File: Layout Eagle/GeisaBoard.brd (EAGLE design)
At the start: 87.6 x 63.7 mm, 19 parts, among them X1 22-23-2021

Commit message: GeisaBoard layout completo (espero)
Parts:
- removed Q2: (no value), transistor-power:TO220BV
- removed R3: (no value), rcl:0204/7
- added Q1: IRF540, transistor-power:TO220BV
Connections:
- removed net N$1: DB9.1, Q2.D
- net GND: now also Q1.S; no longer DB9.5
- net LEIRASATIVAS: now also Q1.G; no longer Q2.G
- net N$2: now also DB9.5, Q1.D; no longer Q2.S, R3.1
- net VCC: now also DB9.1; no longer R3.2
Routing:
- net VCC: track 61.4 -> 93.0 mm
- net N$2: track 7.89 -> 28.5 mm
- net N$1: track 15.6 -> 0.00 mm
- net LEIRASATIVAS: track 49.3 -> 43.1 mm
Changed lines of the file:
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@@
 <layers>
 <layer number="1" name="Top" color="4" fill="1" visible="yes" active="yes"/>
-<layer number="16" name="Bottom" color="1" fill="1" visible="no" active="yes"/>
+<layer number="16" name="Bottom" color="1" fill="1" visible="yes" active="yes"/>
 <layer number="17" name="Pads" color="2" fill="1" visible="yes" active="yes"/>
 <layer number="18" name="Vias" color="2" fill="1" visible="yes" active="yes"/>
@@
 <attribute name="OC_NEWARK" value="25C3832" x="78.74" y="37.465" size="1.778" layer="27" rot="R90" display="off"/>
 </element>
-<element name="R3" library="rcl" library_urn="urn:adsk.eagle:library:334" package="0204/7" package3d_urn="urn:adsk.eagle:package:23498/1" value="" x="54.864" y="70.612" rot="R270"/>
-<element name="Q2" library="transistor-power" library_urn="urn:adsk.eagle:library:400" package="TO220BV" package3d_urn="urn:adsk.eagle:package:29484/3" value="" x="59.69" y="70.612" rot="R90"/>
+<element name="Q1" library="transistor-power" library_urn="urn:adsk.eagle:library:400" package="TO220BV" package3d_urn="urn:adsk.eagle:package:29484/3" value="IRF540" x="58.293" y="63.373"/>
 </elements>
 <signals>
-<signal name="GND" class="1">
+<signal name="GND" class="1" airwireshidden="yes">
 <contactref element="ATMEGA" pad="8"/>
 <contactref element="ATMEGA" pad="22"/>
@@
 <contactref element="JACK" pad="GNDBREAK"/>
 <contactref element="BLUETOOTH" pad="4"/>
-<contactref element="DB9" pad="5"/>
 <polygon width="0.1524" layer="16">
 <vertex x="100.838" y="-0.508"/>
@@
 <wire x1="26.67" y1="74.295" x2="26.924" y2="74.8538" width="1.016" layer="1"/>
 <wire x1="6.35" y1="57.785" x2="6.35" y2="57.658" width="1.016" layer="1"/>
+<contactref element="Q1" pad="S"/>
 </signal>
 <signal name="SPI_SCK">
@@
 <signal name="LEIRASATIVAS">
 <contactref element="ATMEGA" pad="11"/>
-<contactref element="Q2" pad="G"/>
 <wire x1="43.815" y1="40.64" x2="39.37" y2="36.195" width="0.508" layer="1"/>
 <wire x1="43.815" y1="62.992" x2="43.815" y2="40.64" width="0.508" layer="1"/>
-<wire x1="45.593" y1="64.77" x2="43.815" y2="62.992" width="0.508" layer="1"/>
-<wire x1="58.928" y1="64.77" x2="45.593" y2="64.77" width="0.508" layer="1"/>
-<wire x1="62.23" y1="68.072" x2="58.928" y2="64.77" width="0.508" layer="1"/>
+<wire x1="43.815" y1="62.992" x2="45.593" y2="64.77" width="0.508" layer="1"/>
 <wire x1="39.37" y1="36.195" x2="39.37" y2="36.068" width="0.508" layer="1"/>
+<contactref element="Q1" pad="G"/>
+<wire x1="51.816" y1="64.77" x2="55.753" y2="60.833" width="0.508" layer="1"/>
+<wire x1="45.593" y1="64.77" x2="51.816" y2="64.77" width="0.508" layer="1"/>
 </signal>
 <signal name="S0">
@@
 <wire x1="27.305" y1="38.735" x2="27.686" y2="39.116" width="0.508" layer="1"/>
 <wire x1="25.4" y1="41.402" x2="27.686" y2="39.116" width="0.508" layer="16"/>
-<wire x1="46.863" y1="58.928" x2="46.99" y2="58.928" width="0.508" layer="16"/>
 <wire x1="46.99" y1="58.928" x2="44.323" y2="58.928" width="0.508" layer="16"/>
 <wire x1="43.688" y1="59.563" x2="43.688" y2="64.135" width="0.508" layer="16"/>
@@
 <wire x1="39.497" y1="48.895" x2="39.37" y2="48.768" width="0.508" layer="1"/>
 <wire x1="44.958" y1="67.056" x2="47.752" y2="67.056" width="0.508" layer="1"/>
-<wire x1="55.88" y1="61.722" x2="76.304" y2="61.722" width="0.508" layer="16"/>
-<wire x1="50.546" y1="67.056" x2="55.88" y2="61.722" width="0.508" layer="16"/>
-<wire x1="47.752" y1="67.056" x2="50.546" y2="67.056" width="0.508" layer="16"/>
+<wire x1="74.295" y1="61.722" x2="76.304" y2="61.722" width="0.508" layer="16"/>
+<wire x1="68.961" y1="67.056" x2="74.295" y2="61.722" width="0.508" layer="16"/>
+<wire x1="47.752" y1="67.056" x2="68.961" y2="67.056" width="0.508" layer="16"/>
 <wire x1="42.545" y1="64.643" x2="44.958" y2="67.056" width="0.508" layer="1"/>
 <wire x1="42.545" y1="51.943" x2="42.545" y2="64.643" width="0.508" layer="1"/>
@@
 <wire x1="46.99" y1="36.068" x2="59.055" y2="36.068" width="0.508" layer="1"/>
 </signal>
-<signal name="VCC" class="1">
+<signal name="VCC" class="1" airwireshidden="yes">
 <contactref element="SD" pad="VCC"/>
 <contactref element="ATMEGA" pad="21"/>
@@
 <contactref element="VCC_LIGAR_BLUETOOTH" pad="MP"/>
 <contactref element="JACK" pad="PWR"/>
-<contactref element="R3" pad="2"/>
 <polygon width="0.1524" layer="1">
 <vertex x="-1.524" y="80.772"/>
@@
 <wire x1="71.882" y1="33.147" x2="67.437" y2="33.147" width="1.016" layer="16"/>
 <wire x1="67.437" y1="33.147" x2="59.436" y2="41.148" width="1.016" layer="16"/>
+<contactref element="DB9" pad="1"/>
+<wire x1="76.304" y1="67.262" x2="68.89" y2="74.676" width="1.016" layer="16"/>
+<wire x1="68.89" y1="74.676" x2="47.752" y2="74.676" width="1.016" layer="16"/>
 </signal>
 <signal name="BLUETOOTH_LIGADO">
@@
 <wire x1="41.275" y1="65.024" x2="41.275" y2="53.213" width="0.508" layer="1"/>
 <wire x1="36.068" y1="70.231" x2="41.275" y2="65.024" width="0.508" layer="1"/>
-<wire x1="9.525" y1="49.022" x2="10.2235" y2="49.7205" width="0.508" layer="1"/>
-<wire x1="6.477" y1="45.974" x2="9.525" y2="49.022" width="0.508" layer="1"/>
-<wire x1="6.223" y1="53.848" x2="10.2235" y2="53.848" width="0.508" layer="1"/>
-<wire x1="10.287" y1="53.848" x2="26.67" y2="70.231" width="0.508" layer="1"/>
+<wire x1="10.2235" y1="49.7205" x2="6.477" y2="45.974" width="0.508" layer="1"/>
+<wire x1="26.67" y1="70.231" x2="10.287" y2="53.848" width="0.508" layer="1"/>
 <wire x1="26.67" y1="70.231" x2="36.068" y2="70.231" width="0.508" layer="1"/>
-<wire x1="10.2235" y1="49.7205" x2="10.2235" y2="53.848" width="0.508" layer="1"/>
-<wire x1="10.2235" y1="53.848" x2="10.287" y2="53.848" width="0" layer="19" extent="1-1"/>
+<wire x1="10.287" y1="53.848" x2="6.223" y2="53.848" width="0.508" layer="1"/>
+<wire x1="10.287" y1="53.848" x2="10.2235" y2="53.7845" width="0.508" layer="1"/>
+<wire x1="10.2235" y1="53.7845" x2="10.2235" y2="49.7205" width="0.508" layer="1"/>
 </signal>
 <signal name="SS_ADC">
@@
 <wire x1="79.144" y1="63.102" x2="79.254" y2="62.992" width="0.508" layer="16"/>
 </signal>
-<signal name="N$1" class="1">
-<contactref element="DB9" pad="1"/>
-<contactref element="Q2" pad="D"/>
-<wire x1="73.025" y1="70.485" x2="62.23" y2="70.485" width="1.016" layer="16"/>
-<wire x1="76.295571875" y1="67.214428125" x2="73.025" y2="70.485" width="1.016" layer="16"/>
-<wire x1="62.23" y1="70.485" x2="62.23" y2="70.612" width="1.016" layer="16"/>
-<wire x1="76.295571875" y1="67.214428125" x2="76.304" y2="67.262" width="1.016" layer="16"/>
-</signal>
-<signal name="N$2">
-<contactref element="R3" pad="1"/>
-<contactref element="Q2" pad="S"/>
-<wire x1="60.96" y1="74.422" x2="54.864" y2="74.422" width="0.508" layer="1"/>
-<wire x1="62.23" y1="73.152" x2="60.96" y2="74.422" width="0.508" layer="1"/>
+<signal name="N$2" class="1">
+<contactref element="DB9" pad="5"/>
+<contactref element="Q1" pad="D"/>
+<wire x1="58.293" y1="60.833" x2="58.293" y2="56.007" width="1.016" layer="16"/>
+<wire x1="58.293" y1="56.007" x2="63.5" y2="50.8" width="1.016" layer="16"/>
+<wire x1="63.5" y1="50.8" x2="73.152" y2="50.8" width="1.016" layer="16"/>
+<wire x1="73.152" y1="50.8" x2="76.327" y2="53.975" width="1.016" layer="16"/>
+<wire x1="76.327" y1="53.975" x2="76.327" y2="56.159" width="1.016" layer="16"/>
+<wire x1="76.327" y1="56.159" x2="76.304" y2="56.182" width="1.016" layer="16"/>
 </signal>
 </signals>

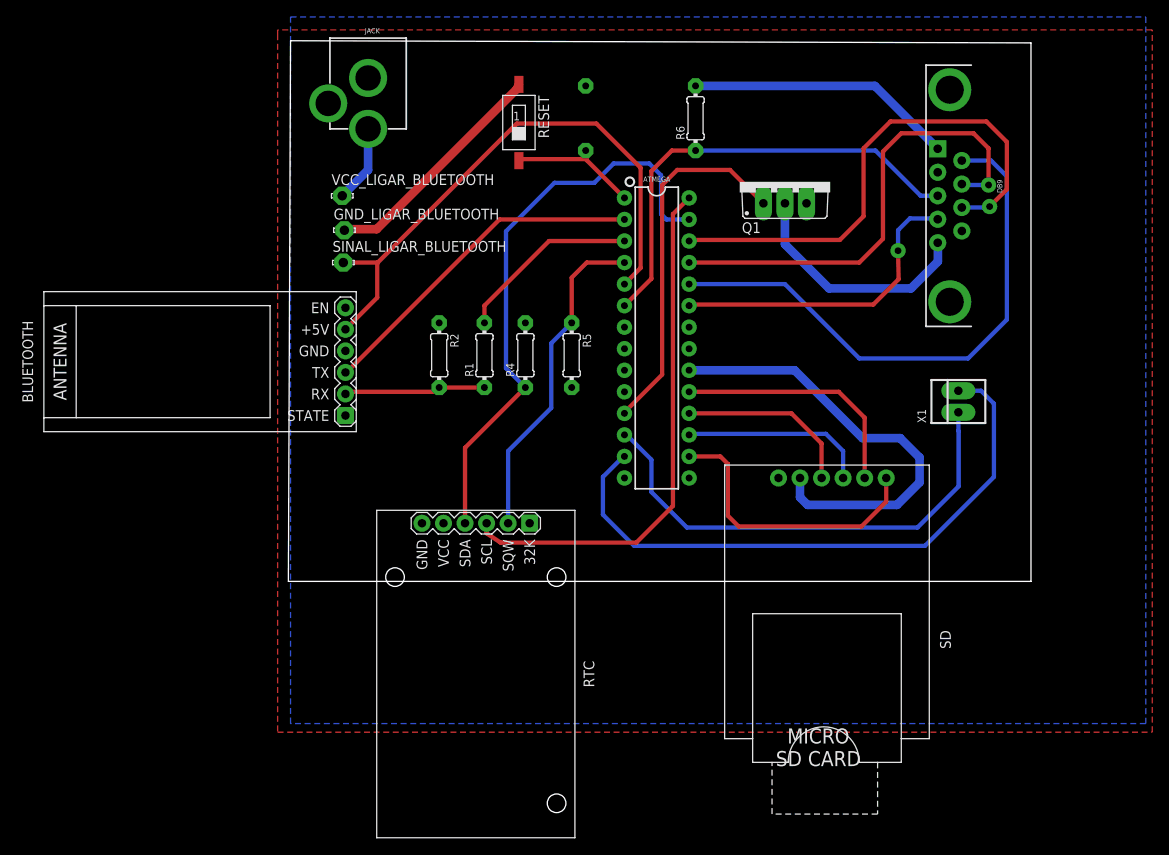
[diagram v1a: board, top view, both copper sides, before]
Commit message: Resistor de pull-down colocado no chaveamento do transistor de potência
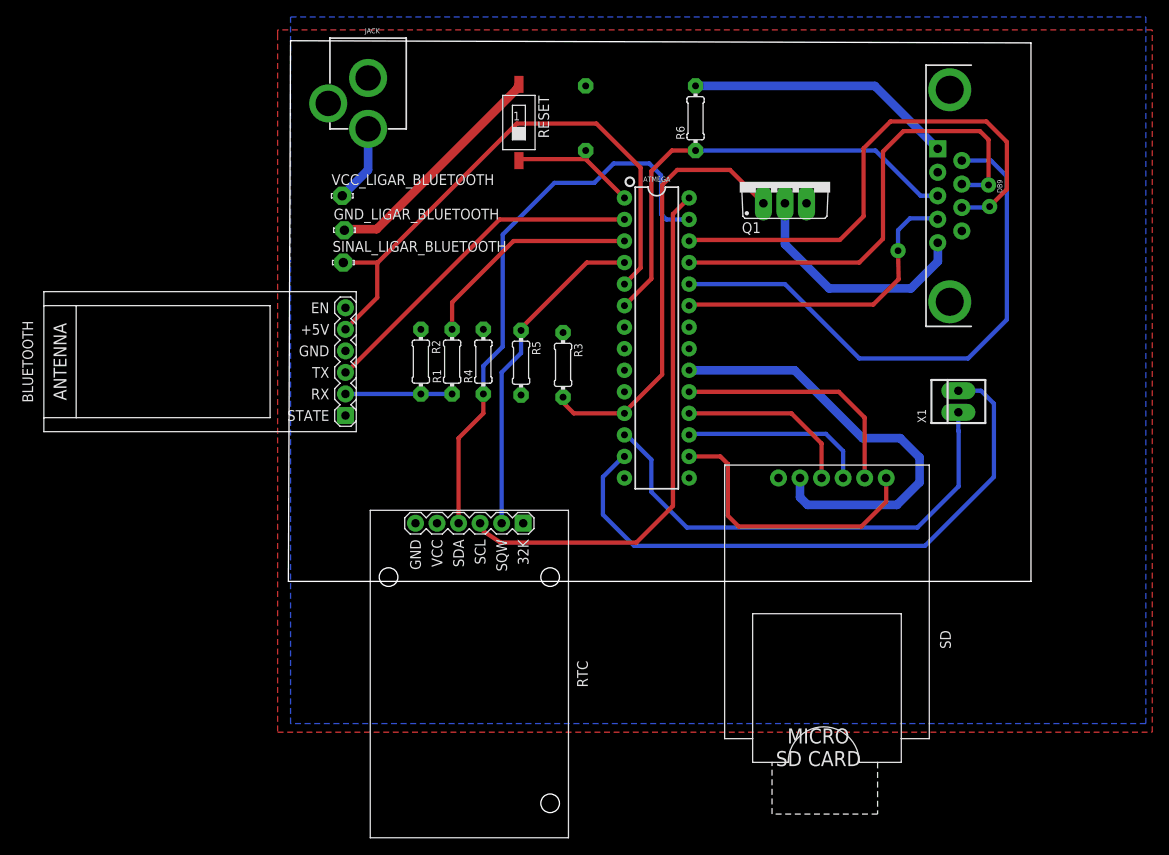
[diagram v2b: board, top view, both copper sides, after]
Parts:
- added R3: 4k7, rcl:0204/7
- moved R5 6.03 mm to (27.2, 42.0)
- moved R4 5.01 mm to (22.7, 42.2)
- moved R1 3.89 mm to (19.1, 42.2)
- moved R2 2.29 mm to (15.4, 42.2)
- moved RTC 0.76 mm to (21.1, 5.33)
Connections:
- net GND: now also R3.1
- net LEIRASATIVAS: now also R3.2
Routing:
- net LEIRASATIVAS: track 43.1 -> 51.5 mm
- net ATM_T_BT_R: track 21.7 -> 26.5 mm
- net 3,3_BT_R: track 16.8 -> 12.6 mm
- net RTC_SDA: track 68.6 -> 67.0 mm
- net DI_ADC: track 55.9 -> 56.7 mm

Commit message: Versão Final da GeisaBoard
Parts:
- added MICRO_USB: (no value), SparkFun-Connectors:USB-B-MICRO-SMD_RED_PASTE
- moved RESET 4.71 mm to (22.4, 71.5)
- moved R9 1.78 mm to (36.6, 70.7)
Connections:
- net GND: now also MICRO_USB.GND
- net VCC: now also MICRO_USB.VBUS
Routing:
- net VCC: track 93.0 -> 100.1 mm
- net GND: track 27.9 -> 34.8 mm
- net RESET/: track 16.4 -> 20.9 mm
- net BLUETOOTH_LIGADO: track 68.0 -> 70.3 mm
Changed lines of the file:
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@@
 <layers>
 <layer number="1" name="Top" color="4" fill="1" visible="yes" active="yes"/>
-<layer number="16" name="Bottom" color="1" fill="1" visible="no" active="yes"/>
+<layer number="16" name="Bottom" color="1" fill="1" visible="yes" active="yes"/>
 <layer number="17" name="Pads" color="2" fill="1" visible="yes" active="yes"/>
 <layer number="18" name="Vias" color="2" fill="1" visible="yes" active="yes"/>
@@
 <element name="R4" library="rcl" library_urn="urn:adsk.eagle:library:334" package="0204/7" package3d_urn="urn:adsk.eagle:package:23498/1" value="4k7" x="22.733" y="42.164" rot="R90"/>
 <element name="R5" library="rcl" library_urn="urn:adsk.eagle:library:334" package="0204/7" package3d_urn="urn:adsk.eagle:package:23498/1" value="4k7" x="27.178" y="42.037" rot="R270"/>
-<element name="R9" library="rcl" library_urn="urn:adsk.eagle:library:334" package="0204/7" package3d_urn="urn:adsk.eagle:package:23498/1" value="" x="34.798" y="70.866" rot="MR90"/>
-<element name="RESET" library="smd-special" library_urn="urn:adsk.eagle:library:362" package="SMS-001" package3d_urn="urn:adsk.eagle:package:26467/1" value="SWS001" x="26.924" y="70.358" rot="R180"/>
+<element name="R9" library="rcl" library_urn="urn:adsk.eagle:library:334" package="0204/7" package3d_urn="urn:adsk.eagle:package:23498/1" value="" x="36.576" y="70.739" rot="MR90"/>
+<element name="RESET" library="smd-special" library_urn="urn:adsk.eagle:library:362" package="SMS-001" package3d_urn="urn:adsk.eagle:package:26467/1" value="SWS001" x="22.352" y="71.501" rot="R180"/>
 <element name="DB9" library="SparkFun-Connectors" package="DB9" value="SAIDA" x="77.724" y="61.722" rot="R270">
 <attribute name="PROD_ID" value="CONN-08194" x="77.724" y="61.722" size="1.778" layer="27" rot="R270" display="off"/>
@@
 <element name="Q1" library="transistor-power" library_urn="urn:adsk.eagle:library:400" package="TO220BV" package3d_urn="urn:adsk.eagle:package:29484/3" value="IRF540" x="58.293" y="63.373"/>
 <element name="R3" library="rcl" library_urn="urn:adsk.eagle:library:334" package="0204/7" package3d_urn="urn:adsk.eagle:package:23498/1" value="4k7" x="32.131" y="41.783" rot="R270"/>
+<element name="MICRO_USB" library="SparkFun-Connectors" library_urn="urn:adsk.eagle:library:513" package="USB-B-MICRO-SMD_RED_PASTE" package3d_urn="urn:adsk.eagle:package:38239/1" value="" x="29.972" y="77.089" rot="R270">
+<attribute name="PROD_ID" value="CONN-11752" x="29.972" y="77.089" size="1.778" layer="27" rot="R270" display="off"/>
+</element>
 </elements>
 <signals>
@@
 <vertex x="100.838" y="82.804"/>
 </polygon>
-<wire x1="10.16" y1="57.785" x2="26.67" y2="74.295" width="1.016" layer="1"/>
-<wire x1="6.35" y1="57.785" x2="10.16" y2="57.785" width="1.016" layer="1"/>
-<wire x1="26.67" y1="74.295" x2="26.924" y2="74.8538" width="1.016" layer="1"/>
 <wire x1="6.35" y1="57.785" x2="6.35" y2="57.658" width="1.016" layer="1"/>
 <contactref element="Q1" pad="S"/>
 <contactref element="R3" pad="1"/>
+<contactref element="MICRO_USB" pad="GND"/>
+<wire x1="15.367" y1="66.675" x2="15.367" y2="71.247" width="1.016" layer="1"/>
+<wire x1="6.35" y1="57.658" x2="15.367" y2="66.675" width="1.016" layer="1"/>
+<wire x1="15.367" y1="71.247" x2="20.1168" y2="75.9968" width="1.016" layer="1"/>
+<wire x1="20.1168" y1="75.9968" x2="22.352" y2="75.9968" width="1.016" layer="1"/>
+<wire x1="28.672" y1="74.364" x2="27.333" y2="73.025" width="1.016" layer="1"/>
+<wire x1="24.765" y1="73.025" x2="27.333" y2="73.025" width="1.016" layer="1"/>
+<wire x1="22.352" y1="75.9968" x2="22.352" y2="75.438" width="1.016" layer="1"/>
+<wire x1="22.352" y1="75.438" x2="24.765" y2="73.025" width="1.016" layer="1"/>
 </signal>
 <signal name="SPI_SCK">
@@
 <contactref element="R9" pad="1"/>
 <contactref element="ATMEGA" pad="1"/>
-<wire x1="34.798" y1="66.04" x2="27.305" y2="66.04" width="0.508" layer="1"/>
-<wire x1="34.798" y1="67.056" x2="34.798" y2="66.04" width="0.508" layer="1"/>
-<wire x1="27.305" y1="66.04" x2="26.924" y2="65.8622" width="0.508" layer="1"/>
-<wire x1="34.925" y1="65.913" x2="39.37" y2="61.468" width="0.508" layer="1"/>
-<wire x1="34.925" y1="66.675" x2="34.925" y2="65.913" width="0.508" layer="1"/>
-<wire x1="34.925" y1="66.675" x2="34.798" y2="67.056" width="0.508" layer="1"/>
+<wire x1="36.703" y1="66.929" x2="39.37" y2="64.262" width="0.508" layer="1"/>
+<wire x1="36.576" y1="66.929" x2="22.4282" y2="66.929" width="0.508" layer="1"/>
+<wire x1="22.4282" y1="66.929" x2="22.352" y2="67.0052" width="0.508" layer="1"/>
+<wire x1="36.576" y1="66.929" x2="36.703" y2="66.929" width="0.508" layer="1"/>
+<wire x1="39.37" y1="64.262" x2="39.37" y2="61.468" width="0.508" layer="1"/>
 </signal>
 <signal name="ATM_T_BT_R">
@@
 <wire x1="76.304" y1="67.262" x2="68.89" y2="74.676" width="1.016" layer="16"/>
 <wire x1="68.89" y1="74.676" x2="47.752" y2="74.676" width="1.016" layer="16"/>
+<contactref element="MICRO_USB" pad="VBUS"/>
+<wire x1="31.272" y1="74.364" x2="33.246" y2="72.39" width="1.016" layer="1"/>
+<wire x1="33.246" y1="72.39" x2="34.544" y2="72.39" width="1.016" layer="1"/>
+<wire x1="34.544" y1="72.39" x2="36.576" y2="74.422" width="1.016" layer="1"/>
+<wire x1="36.576" y1="74.422" x2="36.576" y2="74.549" width="1.016" layer="1"/>
 </signal>
 <signal name="BLUETOOTH_LIGADO">
@@
 <wire x1="41.275" y1="53.213" x2="39.37" y2="51.308" width="0.508" layer="1"/>
 <wire x1="41.275" y1="65.024" x2="41.275" y2="53.213" width="0.508" layer="1"/>
-<wire x1="36.068" y1="70.231" x2="41.275" y2="65.024" width="0.508" layer="1"/>
+<wire x1="41.275" y1="65.024" x2="37.084" y2="69.215" width="0.508" layer="1"/>
 <wire x1="10.2235" y1="49.7205" x2="6.477" y2="45.974" width="0.508" layer="1"/>
-<wire x1="26.67" y1="70.231" x2="10.287" y2="53.848" width="0.508" layer="1"/>
-<wire x1="26.67" y1="70.231" x2="36.068" y2="70.231" width="0.508" layer="1"/>
-<wire x1="10.287" y1="53.848" x2="6.223" y2="53.848" width="0.508" layer="1"/>
+<wire x1="10.287" y1="53.848" x2="7.493" y2="53.848" width="0.508" layer="1"/>
 <wire x1="10.287" y1="53.848" x2="10.2235" y2="53.7845" width="0.508" layer="1"/>
 <wire x1="10.2235" y1="53.7845" x2="10.2235" y2="49.7205" width="0.508" layer="1"/>
+<wire x1="7.493" y1="53.848" x2="6.223" y2="53.848" width="0.508" layer="1"/>
+<wire x1="19.177" y1="66.929" x2="19.177" y2="61.468" width="0.508" layer="1"/>
+<wire x1="19.177" y1="61.468" x2="11.557" y2="53.848" width="0.508" layer="1"/>
+<wire x1="11.557" y1="53.848" x2="10.287" y2="53.848" width="0.508" layer="1"/>
+<wire x1="37.084" y1="69.215" x2="21.463" y2="69.215" width="0.508" layer="1"/>
+<wire x1="21.463" y1="69.215" x2="19.177" y2="66.929" width="0.508" layer="1"/>
 </signal>
 <signal name="SS_ADC">

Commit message: Valores de resistores colocados
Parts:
- R1, R7: value (none) -> 4k7
- R2: value (none) -> 9k1
- renumbered R9 to R7
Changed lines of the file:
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@@
 </autorouter>
 <elements>
-<element name="R1" library="rcl" library_urn="urn:adsk.eagle:library:334" package="0204/7" package3d_urn="urn:adsk.eagle:package:23498/1" value="" x="19.05" y="42.164" rot="R90"/>
-<element name="R2" library="rcl" library_urn="urn:adsk.eagle:library:334" package="0204/7" package3d_urn="urn:adsk.eagle:package:23498/1" value="" x="15.367" y="42.164" rot="R270"/>
+<element name="R1" library="rcl" library_urn="urn:adsk.eagle:library:334" package="0204/7" package3d_urn="urn:adsk.eagle:package:23498/1" value="4k7" x="19.05" y="42.164" rot="R90"/>
+<element name="R2" library="rcl" library_urn="urn:adsk.eagle:library:334" package="0204/7" package3d_urn="urn:adsk.eagle:package:23498/1" value="9k1" x="15.367" y="42.164" rot="R270"/>
 <element name="R4" library="rcl" library_urn="urn:adsk.eagle:library:334" package="0204/7" package3d_urn="urn:adsk.eagle:package:23498/1" value="4k7" x="22.733" y="42.164" rot="R90"/>
 <element name="R5" library="rcl" library_urn="urn:adsk.eagle:library:334" package="0204/7" package3d_urn="urn:adsk.eagle:package:23498/1" value="4k7" x="27.178" y="42.037" rot="R270"/>
-<element name="R9" library="rcl" library_urn="urn:adsk.eagle:library:334" package="0204/7" package3d_urn="urn:adsk.eagle:package:23498/1" value="" x="36.576" y="70.739" rot="MR90"/>
+<element name="R7" library="rcl" library_urn="urn:adsk.eagle:library:334" package="0204/7" package3d_urn="urn:adsk.eagle:package:23498/1" value="4k7" x="36.576" y="70.739" rot="MR90"/>
 <element name="RESET" library="smd-special" library_urn="urn:adsk.eagle:library:362" package="SMS-001" package3d_urn="urn:adsk.eagle:package:26467/1" value="SWS001" x="22.352" y="71.501" rot="R180"/>
 <element name="DB9" library="SparkFun-Connectors" package="DB9" value="SAIDA" x="77.724" y="61.722" rot="R270">
@@
 <signal name="RESET/">
 <contactref element="RESET" pad="2"/>
-<contactref element="R9" pad="1"/>
+<contactref element="R7" pad="1"/>
 <contactref element="ATMEGA" pad="1"/>
 <wire x1="36.703" y1="66.929" x2="39.37" y2="64.262" width="0.508" layer="1"/>
@@
 <contactref element="ATMEGA" pad="7"/>
 <contactref element="ATMEGA" pad="20"/>
-<contactref element="R9" pad="2"/>
+<contactref element="R7" pad="2"/>
 <contactref element="RTC" pad="J1.5"/>
 <contactref element="R5" pad="2"/>
